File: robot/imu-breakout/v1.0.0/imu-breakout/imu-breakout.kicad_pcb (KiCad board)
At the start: 2 copper layers, 4 parts, among them U1 IMU-Breakout_1xAcc(1xSS+1xSPI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, U2 BMI085

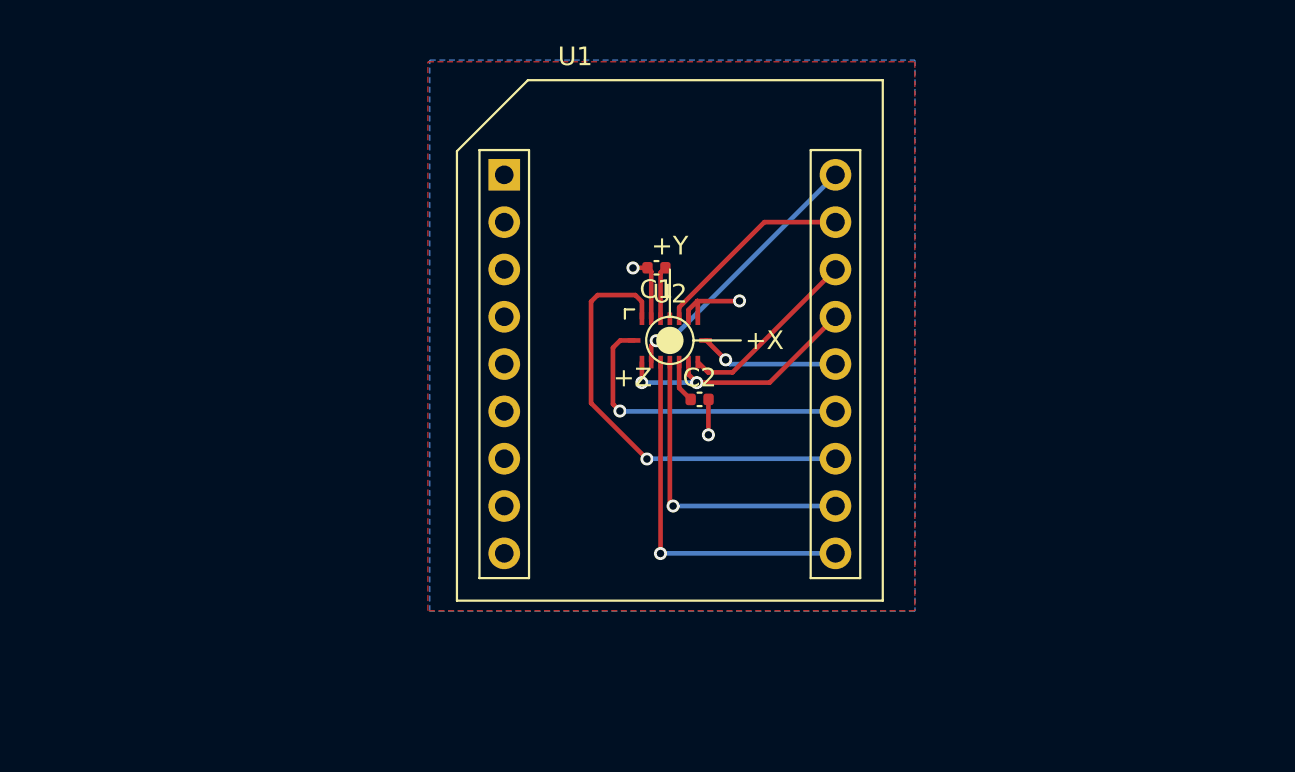
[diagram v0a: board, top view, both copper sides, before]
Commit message: Swap IMU to new connector
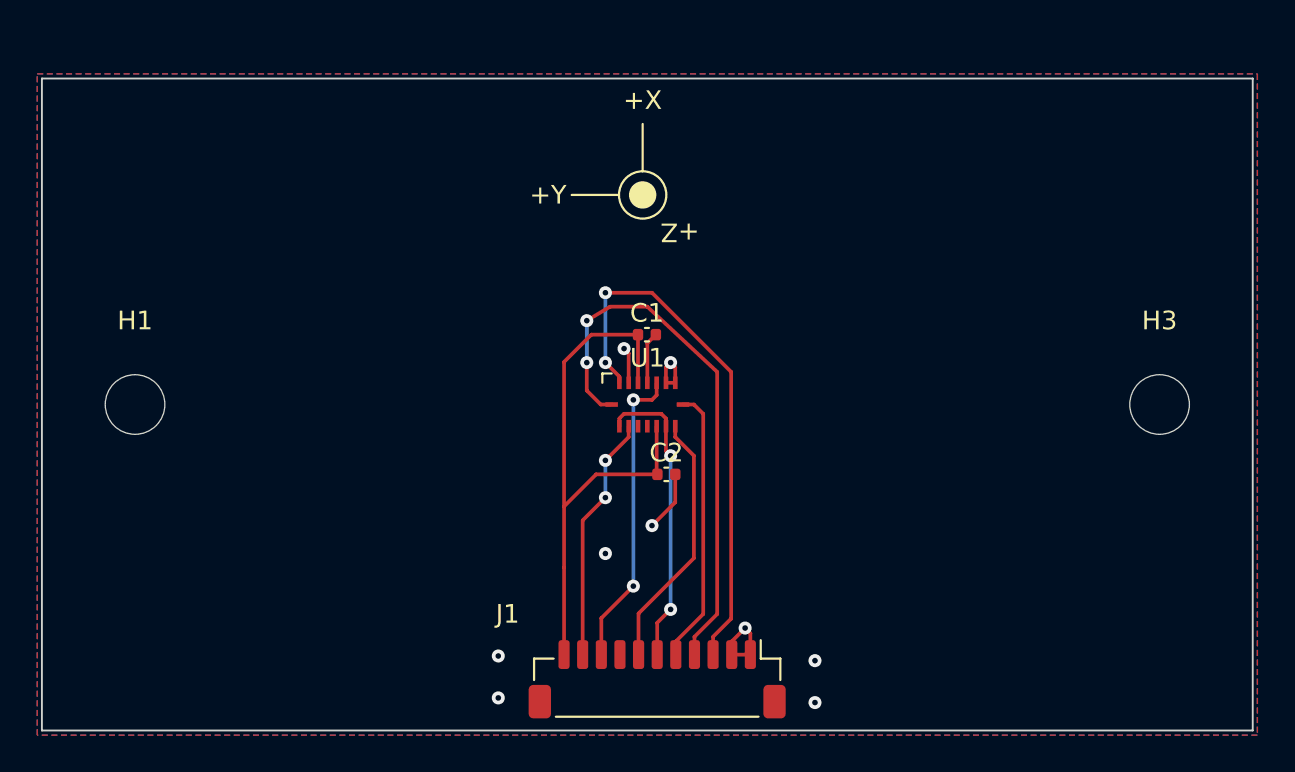
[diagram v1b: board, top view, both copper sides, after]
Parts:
- removed the U1 at (119.4, 86.4)
- added ?: , clipboard:3e92f551-91bf-4371-a95a-b81458c5a9a6, F.Cu at (117.9, 78.5)
- added H1: M3, MountingHole:MountingHole_3.2mm_M3, F.Cu at (90.7, 89.8)
- added H3: M3, MountingHole:MountingHole_3.2mm_M3, F.Cu at (145.7, 89.8)
- added J1: BM11B-SRSS-TB, Connector_JST:JST_SH_BM11B-SRSS-TB_1x11-1MP_P1.00mm_Vertical, F.Cu at (118.7, 104.5)
- moved C2 11.1 mm to (119.2, 93.5), turned to 0 degrees
- moved C1 4.48 mm to (118.2, 86.0)
- moved U1 3.65 mm to (118.2, 89.8)
- renumbered C2 to C1, C1 to C2, U2 to U1
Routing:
- net +3V3: track 5.10 -> 31.2 mm
- net /IMU.INT4: track 19.7 -> 0.00 mm, vias 1 -> 0
- net /IMU.INT3: track 16.5 -> 0.00 mm, vias 1 -> 0
- net /IMU.INT1: track 16.4 -> 29.7 mm, vias 1 -> 2
- net /IMU.SCK: track 7.50 -> 14.8 mm, vias 1 -> 0
- net /IMU.~{SS}2: track 10.9 -> 16.4 mm, vias 0 -> 2
- net /IMU.INT2: track 23.8 -> 29.2 mm, vias 1 -> 2
- net GND: track 9.89 -> 15.1 mm, vias 3 -> 9
- net /IMU.MOSI: track 9.91 -> 13.9 mm
- net /IMU.MISO: track 14.2 -> 16.2 mm
- net /IMU.~{SS}1: track 14.6 -> 13.3 mm, vias 1 -> 2
- added copper zone on F.Cu, net GND
- removed copper zone on F.Cu, net +3V3
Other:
- board outline added: 65 x 35 mm

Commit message: imu updates and gerbers
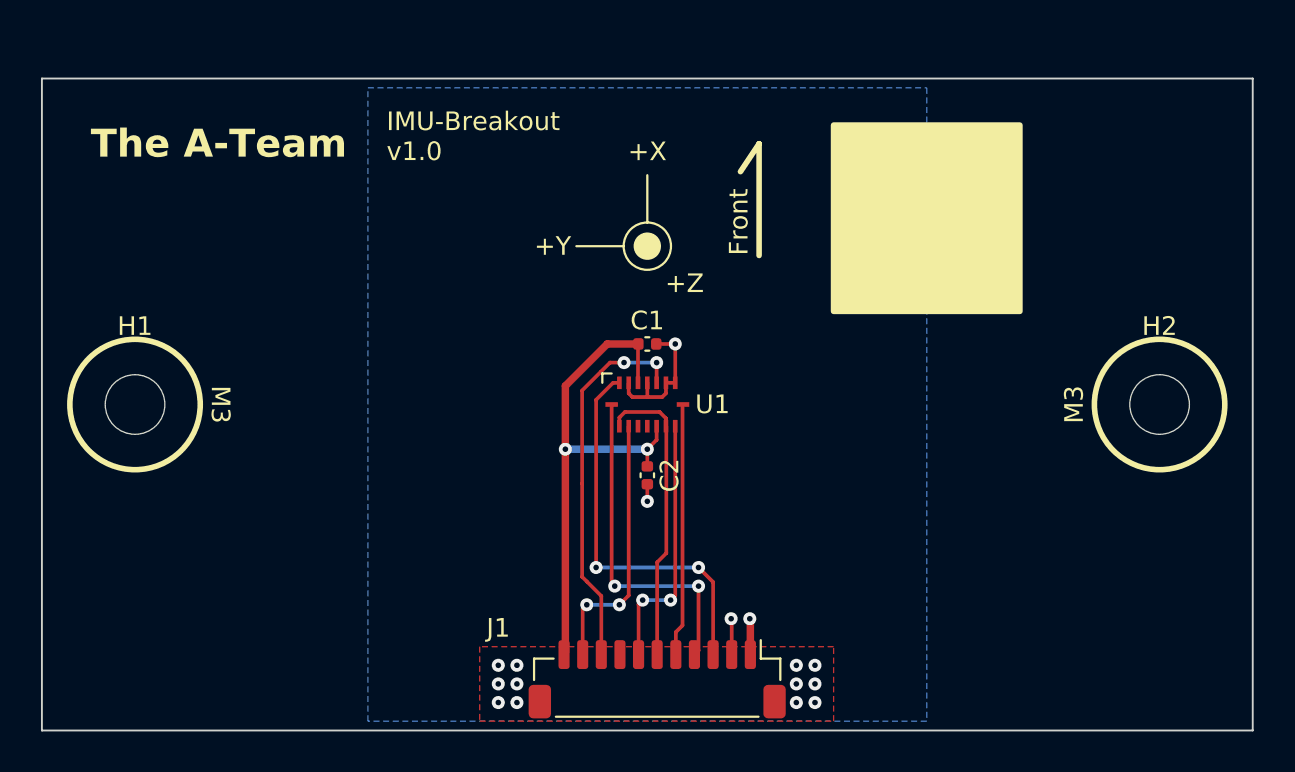
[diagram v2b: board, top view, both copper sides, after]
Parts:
- removed the ? at (117.9, 78.5)
- removed H3: M3, MountingHole:MountingHole_3.2mm_M3
- added ?: , clipboard:72ba34b9-7b15-4069-8230-f829442bcd6c, F.Cu at (118.2, 81.3)
- added H2: M3, MountingHole:MountingHole_3.2mm_M3, F.Cu at (145.7, 89.8)
- moved C2 1.02 mm to (118.2, 93.6), turned to -90 degrees
- moved C1 0.50 mm to (118.2, 86.5)
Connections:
- J1 pad 8: /IMU.~{SS}3 -> unconnected-(J1-Pin_8-Pad8)
- U1 pad 12: /IMU.INT3 -> unconnected-(U1-INT3-Pad12)
- U1 pad 13: /IMU.INT4 -> unconnected-(U1-INT4-Pad13)
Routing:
- net /IMU.INT1: track 29.7 -> 18.1 mm
- net /IMU.INT2: track 29.2 -> 21.1 mm
- net /IMU.~{SS}2: track 16.4 -> 20.3 mm
- net +3V3: track 31.2 -> 28.2 mm, vias 0 -> 2
- net GND: track 15.1 -> 12.5 mm, vias 9 -> 16
- net /IMU.SCK: track 14.8 -> 13.6 mm
- net /IMU.~{SS}1: track 13.3 -> 14.3 mm
- net /IMU.MISO: track 16.2 -> 16.1 mm, vias 2 -> 0
- net /IMU.MOSI: track 13.9 -> 14.0 mm, vias 0 -> 2
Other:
- board text added: "Front"
- board text added: "IMU-Breakout v1.0"
- board text added: "M3"
- board text added: "The A-Team"
